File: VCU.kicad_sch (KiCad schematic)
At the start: 38 parts, among them J1 Conn_02x03_Top_Bottom, J2 2x3_Conn, J3 USB_C_Receptacle_USB2.0_14P, J4 Conn_01x02, SW1 SW_Push, SW2 SW_Push, U1 ESP32-S3-WROOM-1, U2 LM1117DT-3.3, U3 SN65HVD230, U4 USBLC6-2SC6, U6 MCP6001-OT

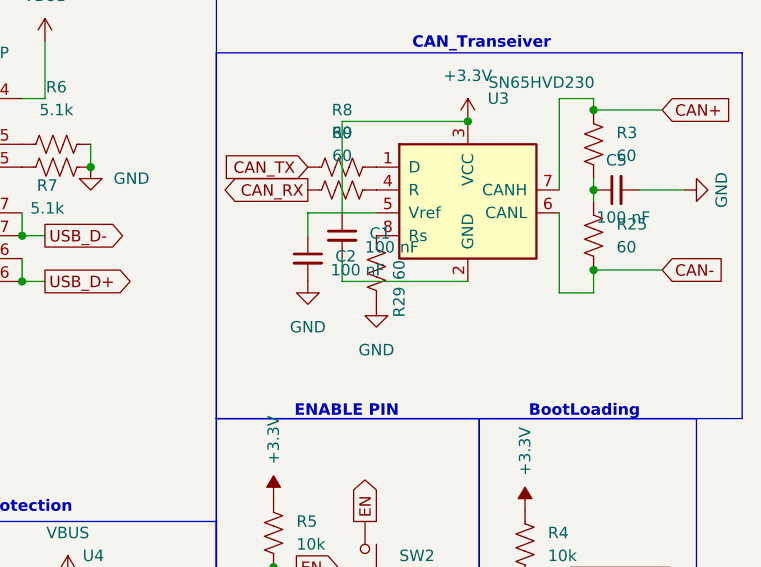
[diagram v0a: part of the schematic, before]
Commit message: Add silkscreen Labels, Add gnd pin to CANTrans
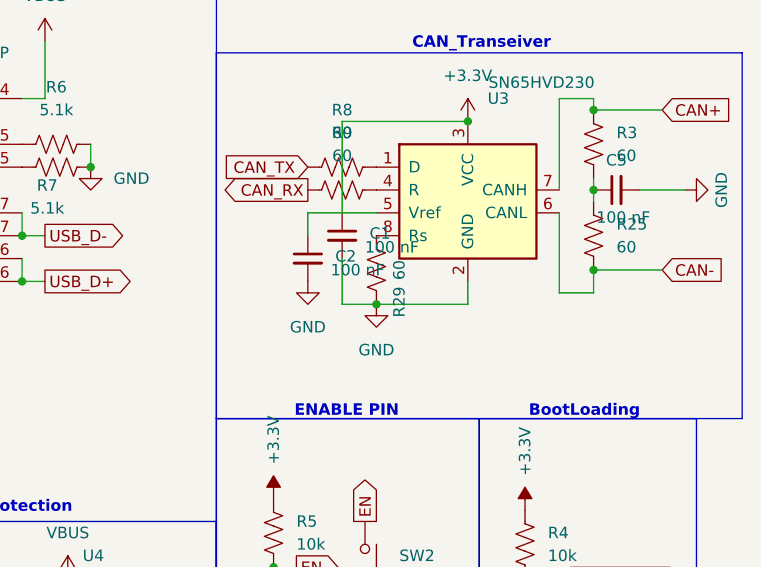
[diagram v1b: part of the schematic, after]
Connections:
- net GND: now also C1.2, U3.2 (GND)
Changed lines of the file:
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@@
+	)
+	(junction
+		(at 140.97 149.86)
+		(diameter 0)
+		(color 0 0 0 0)
 	)
 	(junction
@@
 	(wire
 		(pts
+			(xy 140.97 149.86) (xy 137.16 149.86)
+		)
+		(stroke
+			(width 0)
+			(type default)
+		)
+	)
+	(wire
+		(pts
 			(xy 104.14 120.65) (xy 104.14 127)
 		)
@@
 	(wire
 		(pts
-			(xy 151.13 147.32) (xy 137.16 147.32)
+			(xy 151.13 149.86) (xy 140.97 149.86)
 		)
 		(stroke
@@
 	(wire
 		(pts
-			(xy 137.16 144.78) (xy 137.16 147.32)
+			(xy 137.16 144.78) (xy 137.16 149.86)
 		)
 		(stroke
@@
 		)
 		(stroke
+			(width 0)
+			(type default)
+		)
+	)
+	(wire
+		(pts
+			(xy 151.13 149.86) (xy 151.13 147.32)
+		)
+		(stroke
